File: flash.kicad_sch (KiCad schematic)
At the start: 13 parts, among them U1 LFE5U-85F-6BG381C, U10 IS25LP128F-JBLE

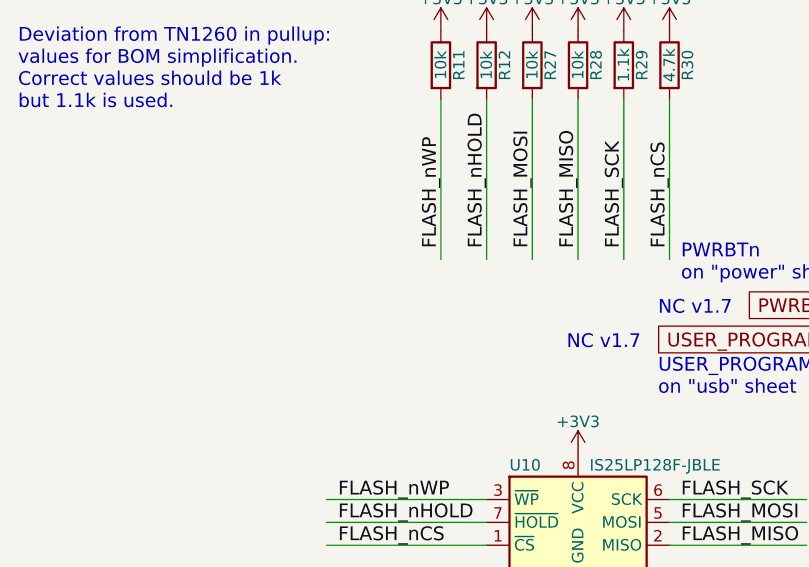
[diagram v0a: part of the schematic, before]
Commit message: use more via in pads
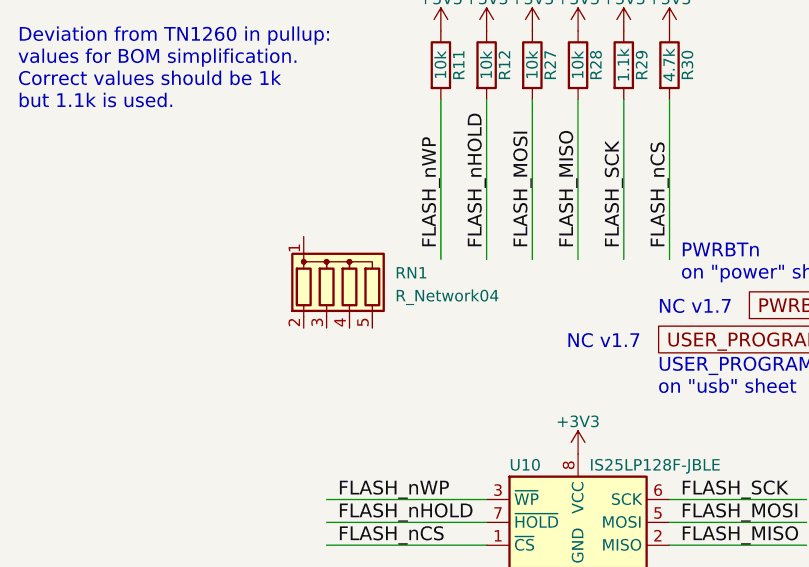
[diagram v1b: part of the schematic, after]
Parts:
- added RN1: R_Network04, Resistor_SMD:R_Array_Convex_4x0402, symbol Device:R_Network04
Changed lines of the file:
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@@
+		)
+	)
+	(symbol
+		(lib_id "Device:R_Network04")
+		(at 67.31 83.82 0)
+		(unit 1)
+		(body_style 1)
+		(exclude_from_sim no)
+		(in_bom yes)
+		(on_board yes)
+		(in_pos_files yes)
+		(dnp no)
+		(fields_autoplaced yes)
+		(property "Reference" "RN1"
+			(at 72.39 82.8039 0)
+			(show_name no)
+			(do_not_autoplace no)
+			(effects
+				(font
+					(size 1.27 1.27)
+				)
+				(justify left)
+			)
+		)
+		(property "Value" "R_Network04"
+			(at 72.39 85.3439 0)
+			(show_name no)
+			(do_not_autoplace no)
+			(effects
+				(font
+					(size 1.27 1.27)
+				)
+				(justify left)
+			)
+		)
+		(property "Footprint" "Resistor_SMD:R_Array_Convex_4x0402"
+			(at 74.295 83.82 90)
+			(hide yes)
+			(show_name no)
+			(do_not_autoplace no)
+			(effects
+				(font
+					(size 1.27 1.27)
+				)
+			)
+		)
+		(property "Datasheet" "http://www.vishay.com/docs/31509/csc.pdf"
+			(at 67.31 83.82 0)
+			(hide yes)
+			(show_name no)
+			(do_not_autoplace no)
+			(effects
+				(font
+					(size 1.27 1.27)
+				)
+			)
+		)
+		(property "Description" "4 resistor network, star topology, bussed resistors, small symbol"
+			(at 67.31 83.82 0)
+			(hide yes)
+			(show_name no)
+			(do_not_autoplace no)
+			(effects
+				(font
+					(size 1.27 1.27)
+				)
+			)
+		)
+		(pin "3"
+		)
+		(pin "1"
+		)
+		(pin "4"
+		)
+		(pin "2"
+		)
+		(pin "5"
+		)
+		(instances
+			(project "ulx3s"
+				(path "/49a43414-f3c1-43b2-ad20-ac3166075f21/00000000-0000-0000-0000-000058d913ec"
+					(reference "RN1")
+					(unit 1)
+				)
+			)
 		)
 	)
